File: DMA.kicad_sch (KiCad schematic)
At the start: 11 parts

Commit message: some clean up and simplification, as well as some renaming
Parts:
- gave numbers to parts that had none: 9
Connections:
- net AB_{0} renamed AB0
- net AB_{10} renamed AB10
- net AB_{11} renamed AB11
- net AB_{12} renamed AB12
- net AB_{13} renamed AB13
- net AB_{14} renamed AB14
- net AB_{15} renamed AB15
- net AB_{1} renamed AB1
- net AB_{2} renamed AB2
- net AB_{3} renamed AB3
- net AB_{4} renamed AB4
- net AB_{5} renamed AB5
- net AB_{6} renamed AB6
- net AB_{7} renamed AB7
- net AB_{8} renamed AB8
- net AB_{9} renamed AB9
- net DB_{0} renamed DB0
- net DB_{1} renamed DB1
- net DB_{2} renamed DB2
- net DB_{3} renamed DB3
- net DB_{4} renamed DB4
- net DB_{5} renamed DB5
- net DB_{6} renamed DB6
- net DB_{7} renamed DB7

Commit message: begin integration of logic into atf1508
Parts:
- U44: footprint (none) -> Package_SO:TSSOP-16_4.4x5mm_P0.65mm
- U45, U47: footprint (none) -> Package_TO_SOT_SMD:SOT-353_SC-70-5
- U46, U48: footprint (none) -> Package_SO:TSSOP-20_4.4x6.5mm_P0.65mm
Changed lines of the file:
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@@
     (property "Reference" "U45" (id 0) (at 139.065 142.875 0))
     (property "Value" "74LVC1G32" (id 1) (at 139.065 145.415 0))
-    (property "Footprint" "" (id 2) (at 146.05 139.7 0)
+    (property "Footprint" "Package_TO_SOT_SMD:SOT-353_SC-70-5" (id 2) (at 146.05 139.7 0)
       (effects (font (size 1.27 1.27)) hide)
     )
@@
       (effects (font (size 1.27 1.27)) (justify left))
     )
-    (property "Footprint" "" (id 2) (at 241.3 127 0)
+    (property "Footprint" "Package_SO:TSSOP-20_4.4x6.5mm_P0.65mm" (id 2) (at 241.3 127 0)
       (effects (font (size 1.27 1.27)) hide)
     )
@@
       (effects (font (size 1.27 1.27)) (justify left))
     )
-    (property "Footprint" "" (id 2) (at 177.8 127 0)
+    (property "Footprint" "Package_SO:TSSOP-20_4.4x6.5mm_P0.65mm" (id 2) (at 177.8 127 0)
       (effects (font (size 1.27 1.27)) hide)
     )
@@
     (property "Reference" "U44" (id 0) (at 50.8 112.395 0))
     (property "Value" "74LS139" (id 1) (at 50.8 114.935 0))
-    (property "Footprint" "" (id 2) (at 50.8 123.19 0)
+    (property "Footprint" "Package_SO:TSSOP-16_4.4x5mm_P0.65mm" (id 2) (at 50.8 123.19 0)
       (effects (font (size 1.27 1.27)) hide)
     )
@@
     (property "Reference" "U44" (id 0) (at 139.065 177.165 0))
     (property "Value" "74LS139" (id 1) (at 139.065 179.705 0))
-    (property "Footprint" "" (id 2) (at 139.065 187.96 0)
+    (property "Footprint" "Package_SO:TSSOP-16_4.4x5mm_P0.65mm" (id 2) (at 139.065 187.96 0)
       (effects (font (size 1.27 1.27)) hide)
     )
@@
       (effects (font (size 1.27 1.27)) (justify left))
     )
-    (property "Footprint" "" (id 2) (at 166.37 178.435 0)
+    (property "Footprint" "Package_SO:TSSOP-16_4.4x5mm_P0.65mm" (id 2) (at 166.37 178.435 0)
       (effects (font (size 1.27 1.27)) hide)
     )
@@
     (property "Reference" "U47" (id 0) (at 202.565 140.335 0))
     (property "Value" "74LVC1G32" (id 1) (at 202.565 142.875 0))
-    (property "Footprint" "" (id 2) (at 209.55 137.16 0)
-      (effects (font (size 1.27 1.27)) hide)
-    )
+    (property "Footprint" "Package_TO_SOT_SMD:SOT-353_SC-70-5" (id 2) (at 209.55 137.16 0)
+      (effects (font (size 1.27 1.27)) hide)
+    )

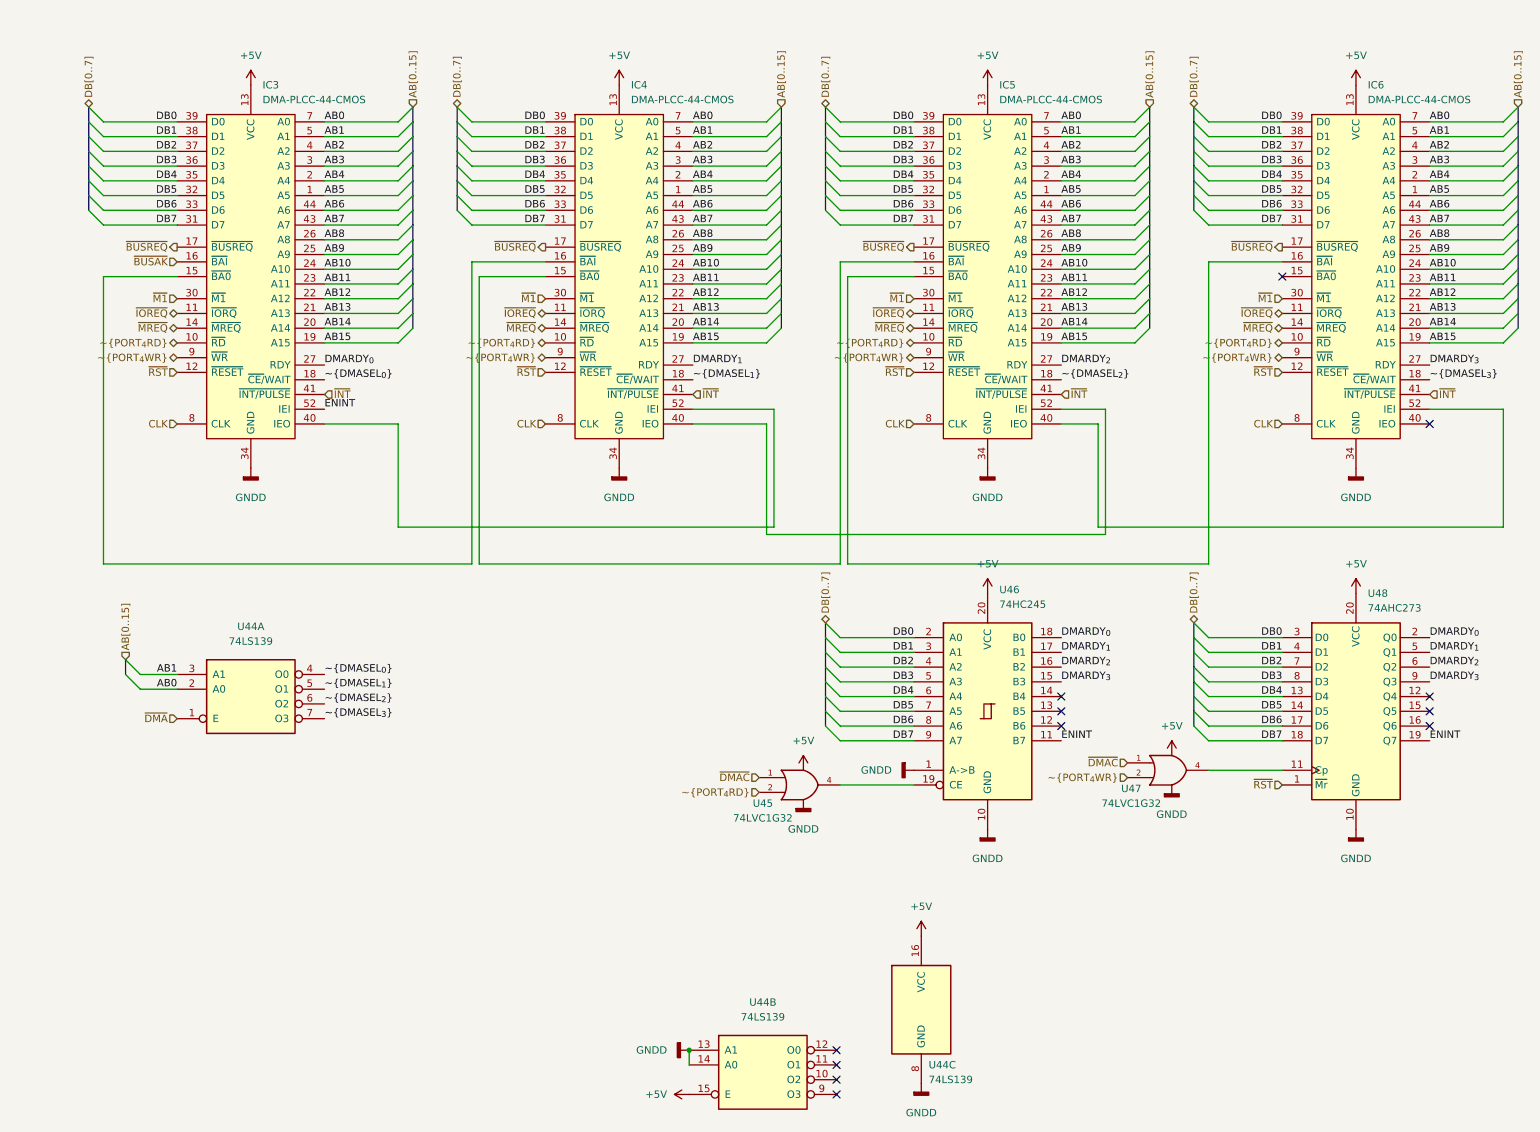
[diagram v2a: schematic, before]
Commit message: added ATF150x part (specifically the 1508) vhdl file contains the (hopeful) implementition of the mapper
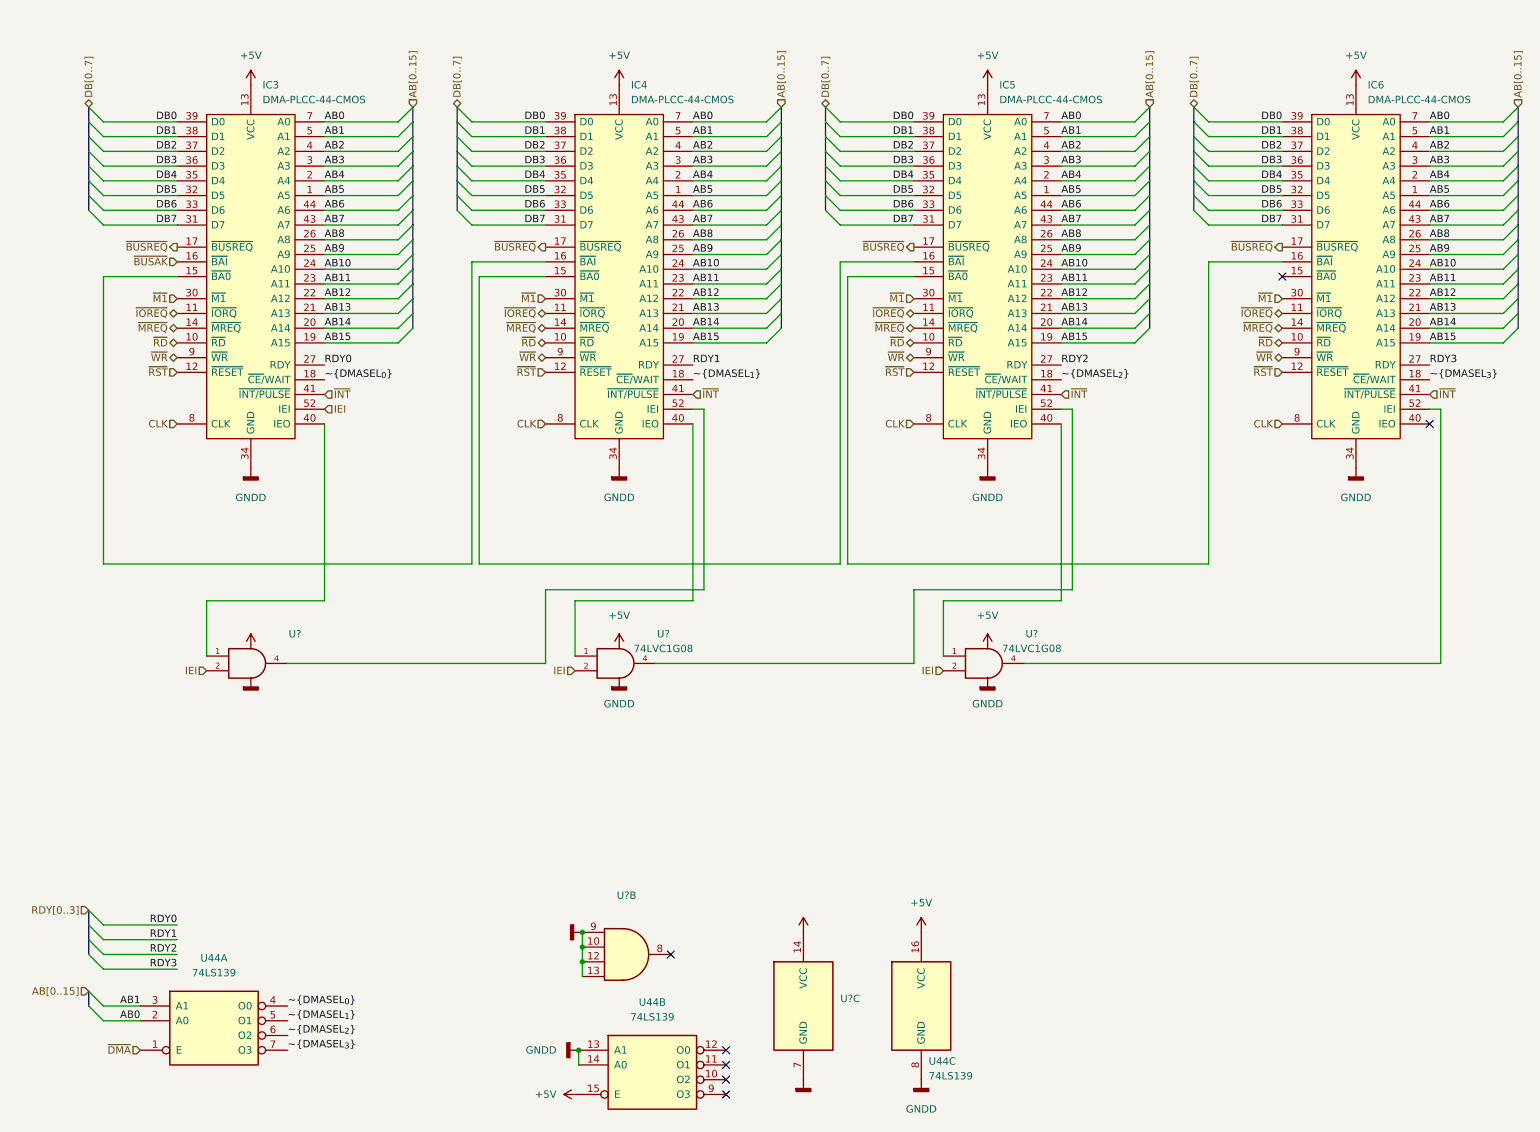
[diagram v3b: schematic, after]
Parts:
- removed U45, U47: 74LVC1G32, Package_TO_SOT_SMD:SOT-353_SC-70-5, symbol 74xGxx:74LVC1G32
- removed U46: 74HC245, Package_SO:TSSOP-20_4.4x6.5mm_P0.65mm, symbol 74xx:74HC245
- removed U48: 74AHC273, Package_SO:TSSOP-20_4.4x6.5mm_P0.65mm, symbol 74xx:74AHC273
- added U? (x2): (no value), symbol 74xx:74LS21
- added U?: (no value), symbol 74xGxx:74LVC1G08
- added U? (x2): 74LVC1G08, symbol 74xGxx:74LVC1G08
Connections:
- net +5V: now also U?.14 (VCC), U?.5 (VCC), U?.5 (VCC), U?.5 (VCC)
- net GND: now also U?.10, U?.12, U?.13, U?.3 (GND), U?.3 (GND), U?.3 (GND), U?.7 (GND), U?.9
- net at IC4.40 (IEO): now also U?.1; no longer IC5.52 (IEI)
- net at IC4.52 (IEI): now also U?.4; no longer IC3.40 (IEO)
- net at IC5.40 (IEO): now also U?.1; no longer IC6.52 (IEI)
- net DMARDY_{0} renamed RDY0
- net DMARDY_{1} renamed RDY1
- net DMARDY_{2} renamed RDY2
- net DMARDY_{3} renamed RDY3
- net ENINT renamed IEI
- net IEI: now also U?.2, U?.2, U?.2
- net ~{PORT_{4}RD} renamed ~{RD}
- net ~{PORT_{4}WR} renamed ~{WR}
- new net: IC3.40 (IEO), U?.1
- new net: IC5.52 (IEI), U?.4
- new net: IC6.52 (IEI), U?.4
- no-connect marks 12 -> 7
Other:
- moved on the sheet: U44A, U44B, U44C

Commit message: updated 84c10 pinout, apparently never checked for validity.... further simplification of dma and timer system (removed mode 2 interrupt structure, and interrupts in general) cleaned up vhdl code for 1508, still need testing to ensure functionality and that it even fits in the 1508....
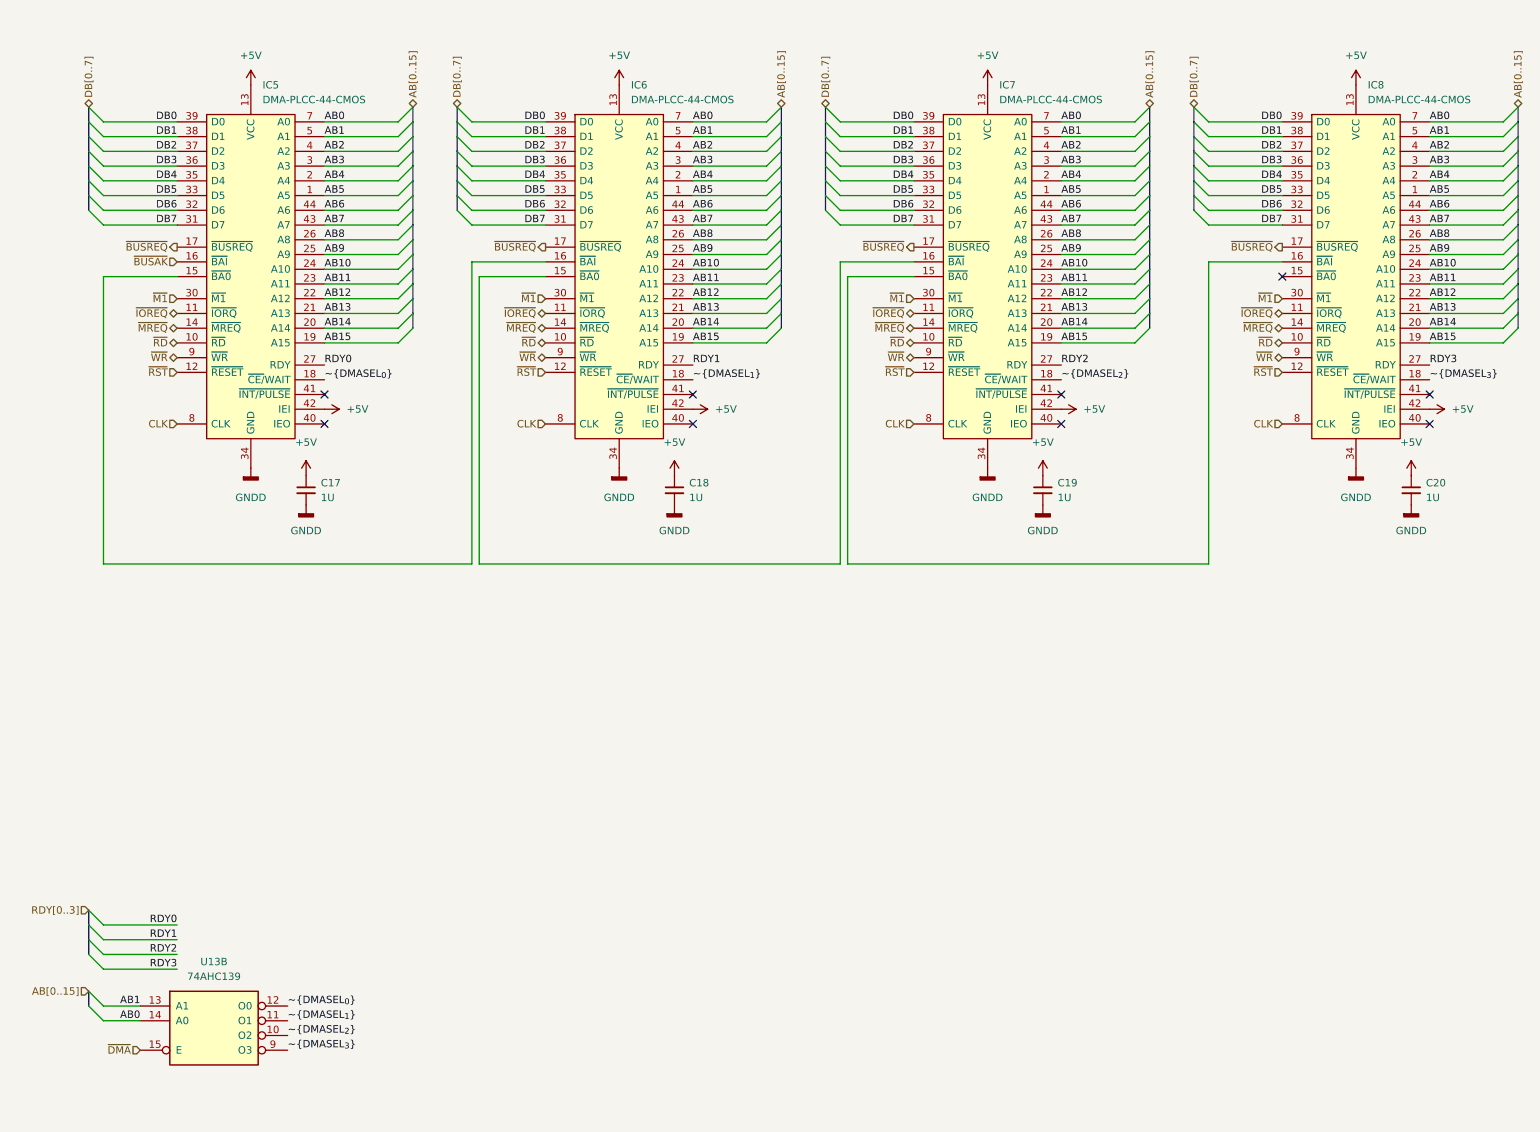
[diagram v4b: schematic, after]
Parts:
- removed U44: 74LS139, Package_SO:TSSOP-16_4.4x5mm_P0.65mm, symbol 74xx:74LS139
- removed U? (x2): (no value), symbol 74xx:74LS21
- removed U?: (no value), symbol 74xGxx:74LVC1G08
- removed U? (x2): 74LVC1G08, symbol 74xGxx:74LVC1G08
- added C17, C18, C19, C20: 1U, Capacitor_SMD:C_1206_3216Metric, symbol Device:C_Small
- added U13: 74AHC139, Package_SO:TSSOP-16_4.4x5mm_P0.65mm, symbol 74xx:74LS139
- renumbered IC3 to IC5, IC4 to IC6, IC5 to IC7, IC6 to IC8
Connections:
- net +5V: now also IC5.42 (IEI), IC6.42 (IEI), IC7.42 (IEI), IC8.42 (IEI), C17.1, C18.1, C19.1, C20.1
- net AB0: now also U13.14 (A0)
- net AB1: now also U13.13 (A1)
- net DB5: now also IC5.33 (D5), IC6.33 (D5), IC7.33 (D5), IC8.33 (D5); no longer IC5.32 (D5), IC6.32 (D5), IC7.32 (D5), IC8.32 (D5)
- net DB6: now also IC5.32 (D6), IC6.32 (D6), IC7.32 (D6), IC8.32 (D6); no longer IC5.33 (D6), IC6.33 (D6), IC7.33 (D6), IC8.33 (D6)
- net ~{DMASEL_{0}}: now also U13.12 (O0)
- net ~{DMASEL_{1}}: now also U13.11 (O1)
- net ~{DMASEL_{2}}: now also U13.10 (O2)
- net ~{DMASEL_{3}}: now also U13.9 (O3)
- net ~{DMA}: now also U13.15 (E)
- net GND renamed GNDD
- net GNDD: now also C17.2, C18.2, C19.2, C20.2
- removed net IEI: IC5.52 (IEI)
- removed net ~{INT}: IC5.41 (~{INT/PULSE}), IC6.41 (~{INT/PULSE}), IC7.41 (~{INT/PULSE}), IC8.41 (~{INT/PULSE})
- no-connect marks 7 -> 9

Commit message: final hardware revision
final update to the hardware:
- removed flash
- added battery backup switch-over
- increased ram to 4MB
- added ramboot/netboot option by using reads to write-only ports to trigger/toggle
- fixed a logic bug i should have caught in writes to the mapper registers (using bits 14&15 instead of 1&0)
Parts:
- added C8: 0U1, Capacitor_SMD:C_0603_1608Metric, symbol Device:C_Small
- added unit 2 of U13
- added unit 3 of U13
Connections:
- net +5V: now also C8.1, U13.15 (E), U13.16 (VCC)
- net AB0: now also U13.2 (A0); no longer U13.14 (A0)
- net AB1: now also U13.3 (A1); no longer U13.13 (A1)
- net GNDD: now also C8.2, U13.13 (A1), U13.14 (A0), U13.8 (GND)
- net ~{DMASEL_{0}}: now also U13.4 (O0); no longer U13.12 (O0)
- net ~{DMASEL_{1}}: now also U13.5 (O1); no longer U13.11 (O1)
- net ~{DMASEL_{2}}: now also U13.6 (O2); no longer U13.10 (O2)
- net ~{DMASEL_{3}}: now also U13.7 (O3); no longer U13.9 (O3)
- net ~{DMA}: now also U13.1 (E); no longer U13.15 (E)
- no-connect marks 9 -> 13
